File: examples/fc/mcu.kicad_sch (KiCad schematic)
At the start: 18 parts, among them J2 USB-C, J3 SWD, U3 STM32F405RGT6, Y1 8MHz

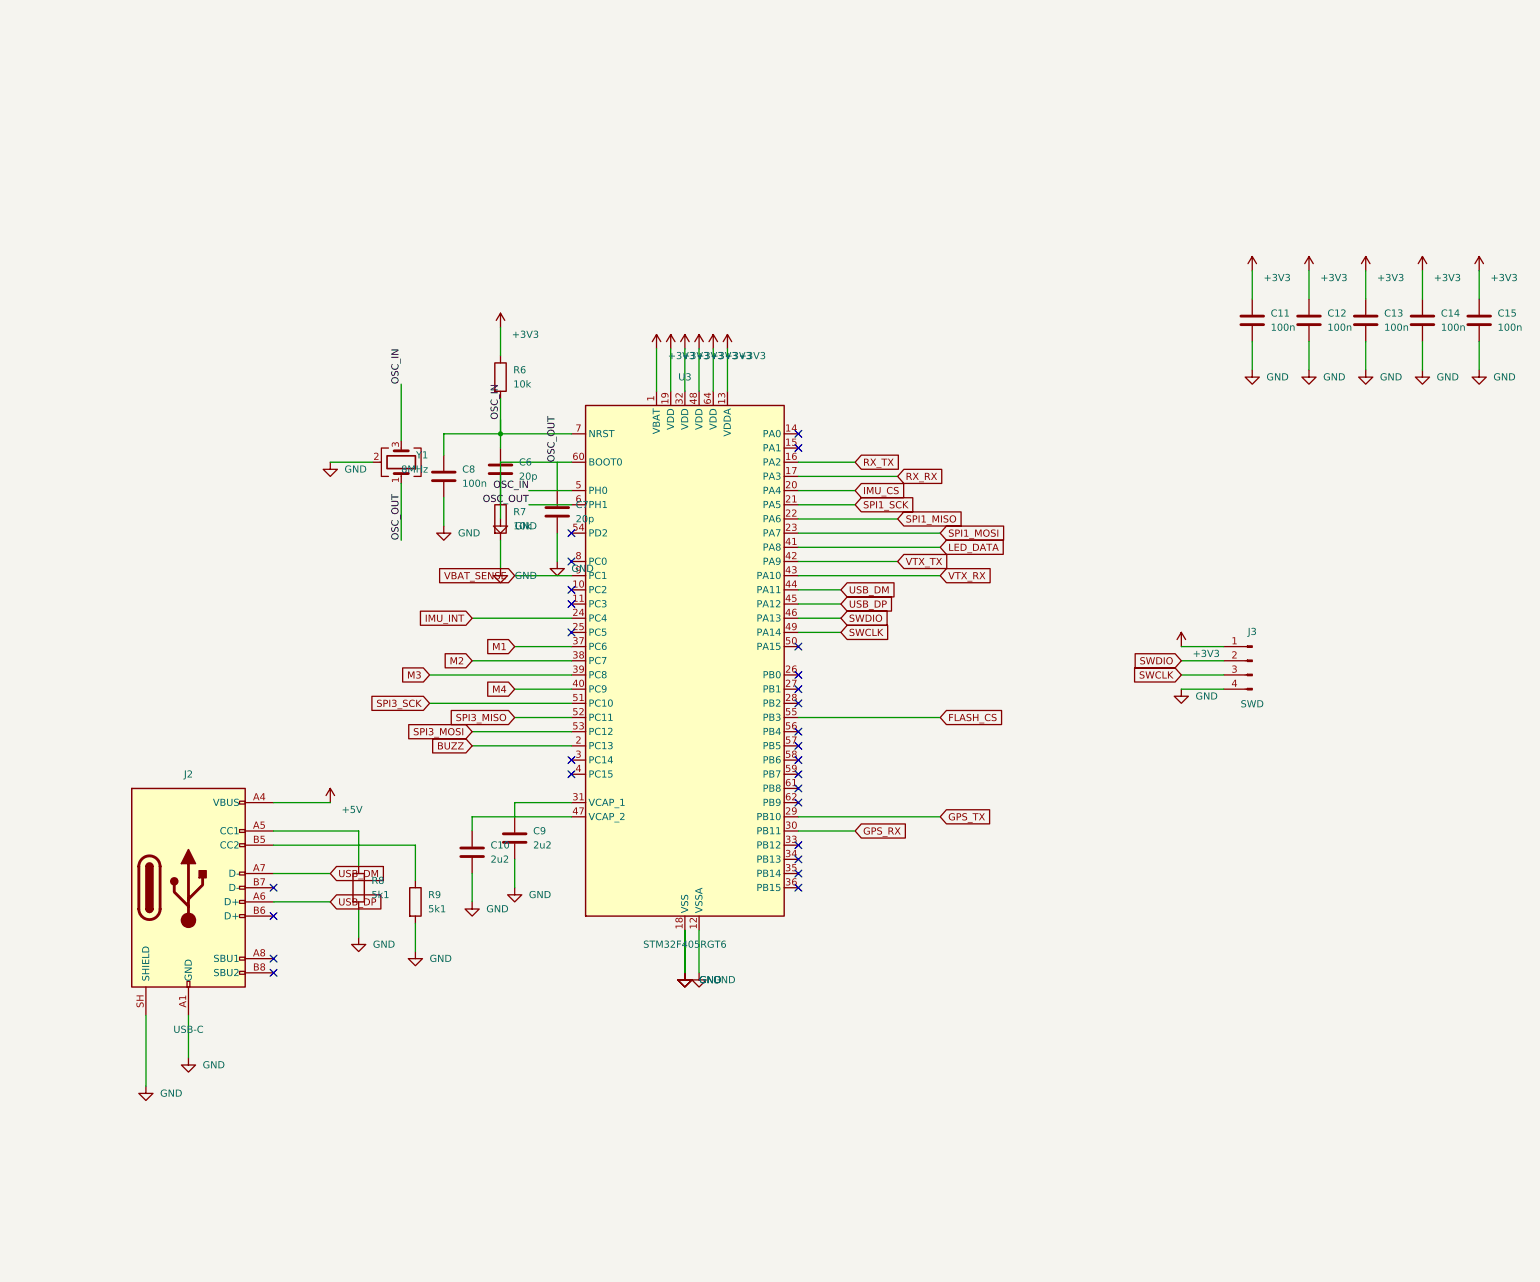
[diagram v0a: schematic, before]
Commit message: Add structured schematic scenes and fix example overlaps
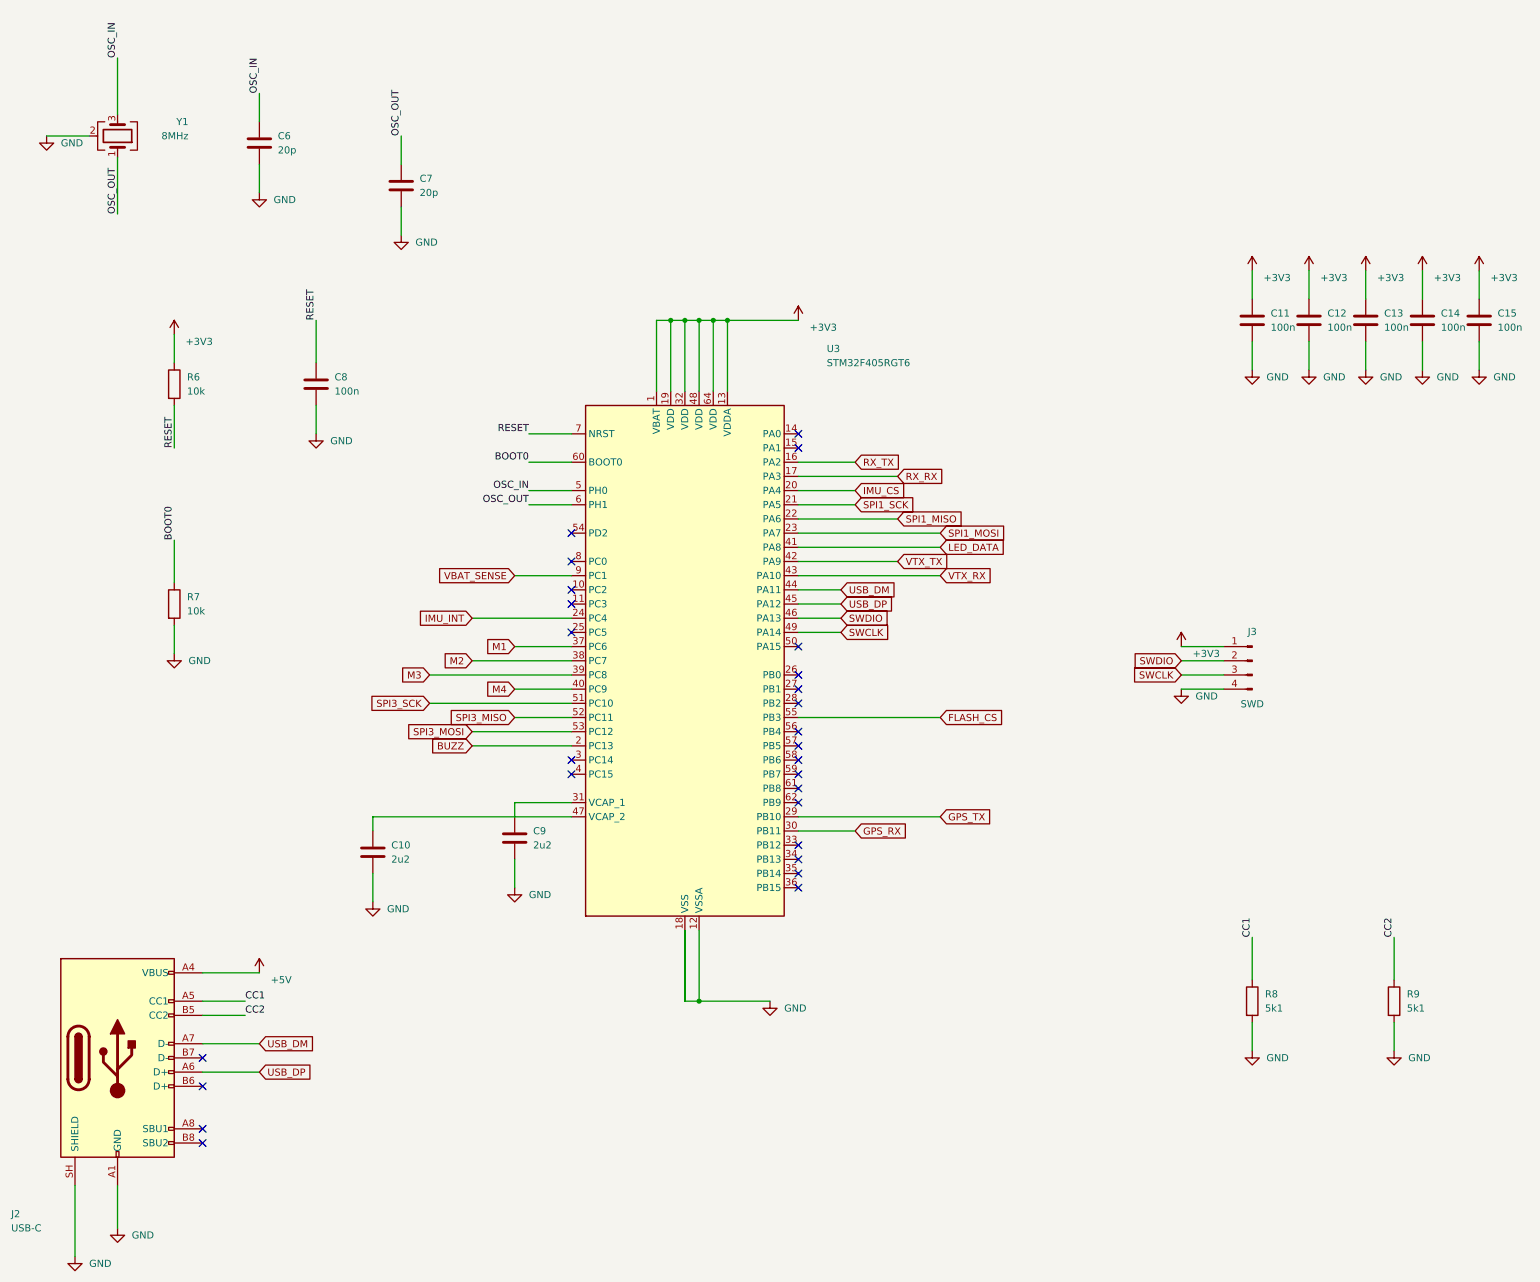
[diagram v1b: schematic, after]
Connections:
- net GND: no longer C7.1, R7.1, U3.6 (PH1), U3.60 (BOOT0), Y1.1
- net OSC_IN: no longer C8.1, R6.2, U3.7 (NRST)
- net CC1: now reaches J2.A5 (CC1), R8.1
- net CC2: now reaches J2.B5 (CC2), R9.1
- new net BOOT0: R7.1, U3.60 (BOOT0)
- new net OSC_OUT: C7.1, U3.6 (PH1), Y1.1
- new net RESET: C8.1, R6.2, U3.7 (NRST)
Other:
- moved on the sheet: C10, C6, C7, C8, J2, R6, R7, R8, R9, Y1
